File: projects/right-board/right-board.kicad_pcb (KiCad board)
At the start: 2 copper layers, 34.1 x 75.7 mm, 6 parts, among them J1 5051101292, SW1 TS06-667-25-BK-160-G-SMT-TR, SW2 TS06-667-25-BK-160-G-SMT-TR, SW3 TS06-667-25-BK-160-G-SMT-TR, SW4 TS06-667-25-BK-160-G-SMT-TR, SW5 TS06-667-25-BK-160-G-SMT-TR

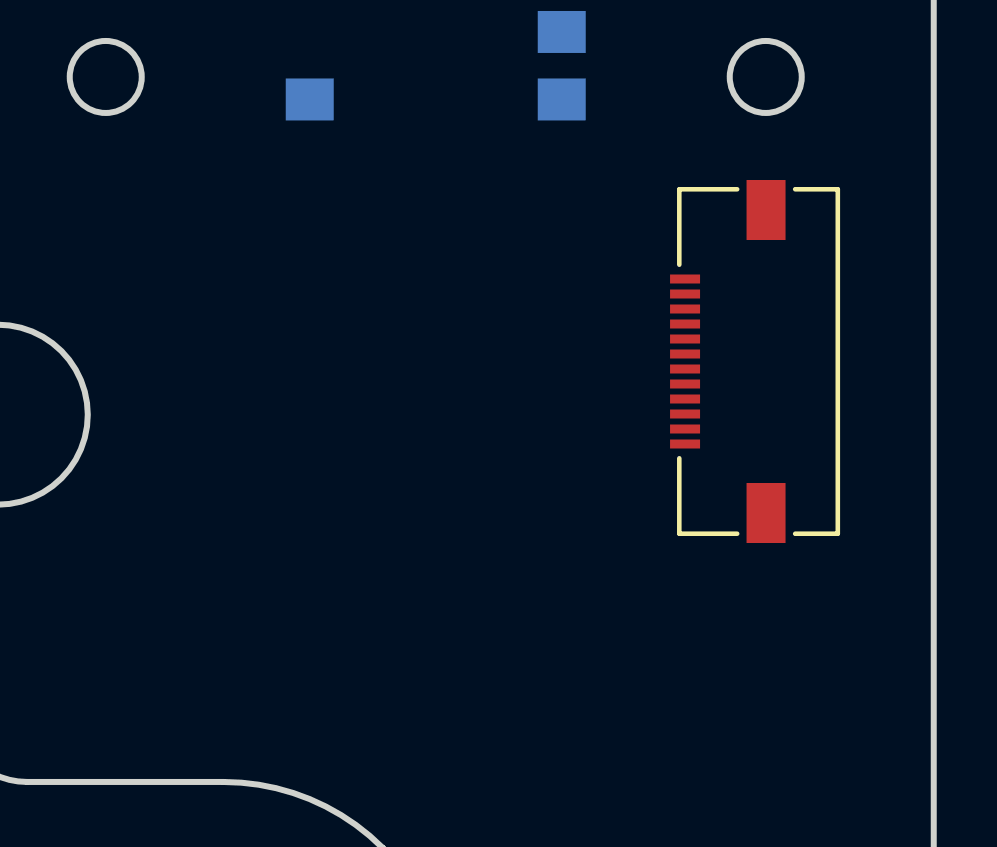
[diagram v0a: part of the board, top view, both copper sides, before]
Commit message: Position board-to-board connectors
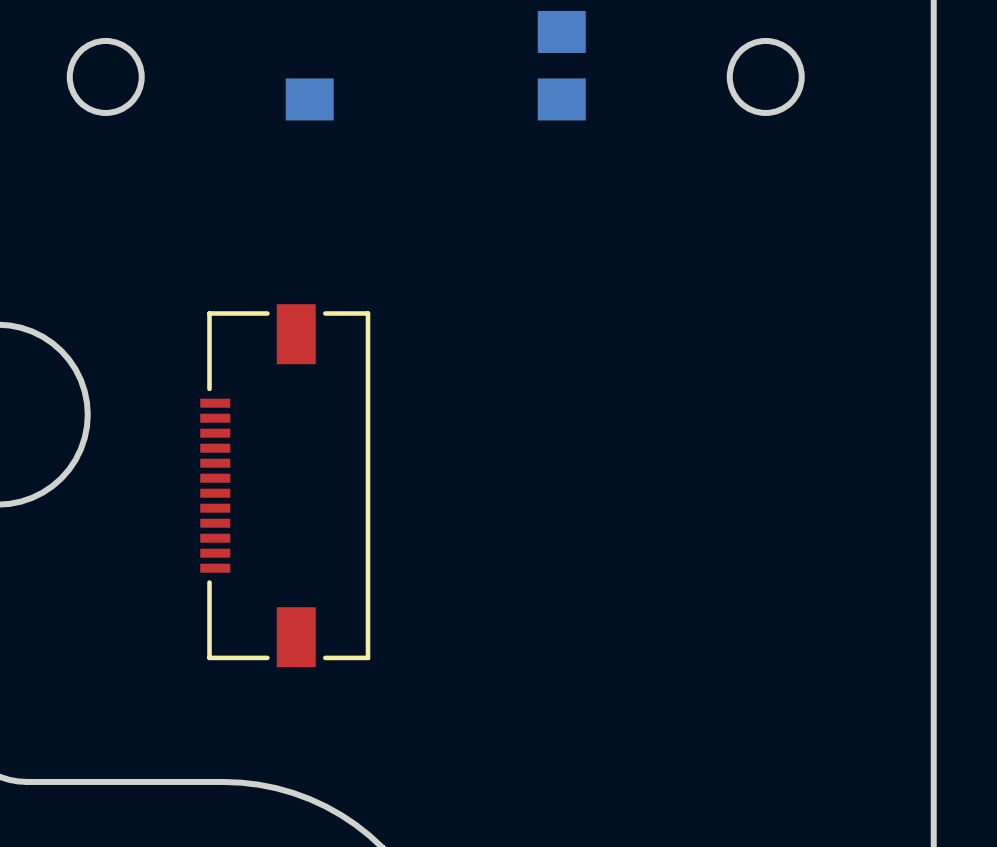
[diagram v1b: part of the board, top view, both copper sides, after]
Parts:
- moved J1 16.2 mm to (151.2, 119.5)
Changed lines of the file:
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@@
 	(footprint "footprint-library:5051101292"
 		(layer "F.Cu")
-		(at 166.88 115.38999 90)
+		(at 151.22 119.53 90)
 		(property "Reference" "J1"
 			(at -0.1016 -6.35 90)
@@
 		(layer "User.1")
 	)
+	(gr_line
+		(start 172.720001 119.53)
+		(end 158.22 119.53)
+		(stroke
+			(width 0.05)
+			(type default)
+		)
+		(layer "User.1")
+	)
+	(gr_line
+		(start 172.720001 96.963978)
+		(end 172.720001 119.53)
+		(stroke
+			(width 0.05)
+			(type default)
+		)
+		(layer "User.1")
+	)
